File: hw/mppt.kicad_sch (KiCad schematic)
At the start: 0 parts

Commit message: working on documentation, design methmethodology, sizing, layout
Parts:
- added H101: Top Left Mounting Hole, MountingHole:MountingHole_2.2mm_M2, symbol Mechanical:MountingHole
- added H102: Top Right Mounting Hole, MountingHole:MountingHole_2.2mm_M2, symbol Mechanical:MountingHole
- added H103: Bottom Left Mounting Hole, MountingHole:MountingHole_2.2mm_M2, symbol Mechanical:MountingHole
- added H104: Bottom Right Mounting Hole, MountingHole:MountingHole_2.2mm_M2, symbol Mechanical:MountingHole
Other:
- sheet controller ports: added ARR_CURRENT, ARR_VOLTAGE, BATT_CURRENT, BATT_VOLTAGE, PWM; removed none
- sheet converter ports: added SW1, SW2, V_ARR+, V_ARR-, V_BATT+, V_BATT-; removed none
- sheet sensors ports: added +ARR, +BATT, -ARR, -BATT, ARRAY_CURRENT, ARRAY_VOLTAGE, BATTERY_CURRENT, BATTERY_VOLTAGE; removed none

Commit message: parts of gate driver
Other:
- sheet controller ports: added PWM_EN; removed none
- sheet gate_driver ports: added PWM, PWM_EN, SW1_OUT, SW2_OUT; removed none
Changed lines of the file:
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@@
     (comment 3 "Matthew Yu")
   )
+  (wire (pts (xy 81.28 72.39) (xy 83.82 72.39))
+    (stroke (width 0) (type default))
+  )
   (wire (pts (xy 34.29 45.72) (xy 31.75 45.72))
     (stroke (width 0) (type default))
   )
+  (wire (pts (xy 83.82 57.15) (xy 81.28 57.15))
+    (stroke (width 0) (type default))
+  )
+  (wire (pts (xy 83.82 54.61) (xy 80.01 54.61))
+    (stroke (width 0) (type default))
+  )
   (wire (pts (xy 29.21 40.64) (xy 29.21 73.66))
     (stroke (width 0) (type default))
@@
     (stroke (width 0) (type default))
   )
+  (wire (pts (xy 72.39 38.1) (xy 83.82 38.1))
+    (stroke (width 0) (type default))
+  )
   (wire (pts (xy 31.75 78.74) (xy 34.29 78.74))
     (stroke (width 0) (type default))
   )
+  (wire (pts (xy 80.01 54.61) (xy 80.01 69.85))
+    (stroke (width 0) (type default))
+  )
   (wire (pts (xy 72.39 83.82) (xy 83.82 83.82))
     (stroke (width 0) (type default))
@@
     (stroke (width 0) (type default))
   )
+  (wire (pts (xy 81.28 57.15) (xy 81.28 72.39))
+    (stroke (width 0) (type default))
+  )
   (wire (pts (xy 72.39 76.2) (xy 83.82 76.2))
     (stroke (width 0) (type default))
@@
     (stroke (width 0) (type default))
   )
+  (wire (pts (xy 72.39 40.64) (xy 83.82 40.64))
+    (stroke (width 0) (type default))
+  )
   (wire (pts (xy 34.29 71.12) (xy 27.94 71.12))
+    (stroke (width 0) (type default))
+  )
+  (wire (pts (xy 80.01 69.85) (xy 83.82 69.85))
     (stroke (width 0) (type default))
   )
@@
       (effects (font (size 1.27 1.27)) (justify left))
     )
-    (pin "PWM" input (at 34.29 49.53 180)
-      (effects (font (size 1.27 1.27)) (justify left))
+    (pin "PWM" input (at 72.39 38.1 0)
+      (effects (font (size 1.27 1.27)) (justify right))
+    )
+    (pin "PWM_EN" input (at 72.39 40.64 0)
+      (effects (font (size 1.27 1.27)) (justify right))
     )
     (instances
@@
       (effects (font (size 1.27 1.27)) (justify left top))
     )
-    (instances
+    (pin "PWM" input (at 83.82 38.1 180)
+      (effects (font (size 1.27 1.27)) (justify left))
+    )
+    (pin "PWM_EN" input (at 83.82 40.64 180)
+      (effects (font (size 1.27 1.27)) (justify left))
+    )
+    (pin "SW1_OUT" input (at 83.82 54.61 180)
+      (effects (font (size 1.27 1.27)) (justify left))
+    )
+    (pin "SW2_OUT" input (at 83.82 57.15 180)
+      (effects (font (size 1.27 1.27)) (justify left))
+    )
+    (instances

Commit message: layout revision this one is cursed
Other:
- sheet converter ports: added V_SW; removed none
- sheet gate_driver ports: added V_SW; removed none
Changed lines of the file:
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@@
+    (stroke (width 0) (type default))
+  )
+  (wire (pts (xy 125.73 69.85) (xy 121.92 69.85))
+    (stroke (width 0) (type default))
+  )
+  (wire (pts (xy 121.92 57.15) (xy 125.73 57.15))
     (stroke (width 0) (type default))
   )
@@
   )
   (wire (pts (xy 30.48 43.18) (xy 30.48 76.2))
+    (stroke (width 0) (type default))
+  )
+  (wire (pts (xy 125.73 57.15) (xy 125.73 69.85))
     (stroke (width 0) (type default))
   )
@@
       (effects (font (size 1.27 1.27)) (justify left))
     )
+    (pin "V_SW" input (at 121.92 69.85 0)
+      (effects (font (size 1.27 1.27)) (justify right))
+    )
     (instances
       (project "mppt"
@@
       (effects (font (size 1.27 1.27)) (justify left))
     )
-    (instances
+    (pin "V_SW" input (at 121.92 57.15 0)
+      (effects (font (size 1.27 1.27)) (justify right))
+    )
+    (instances

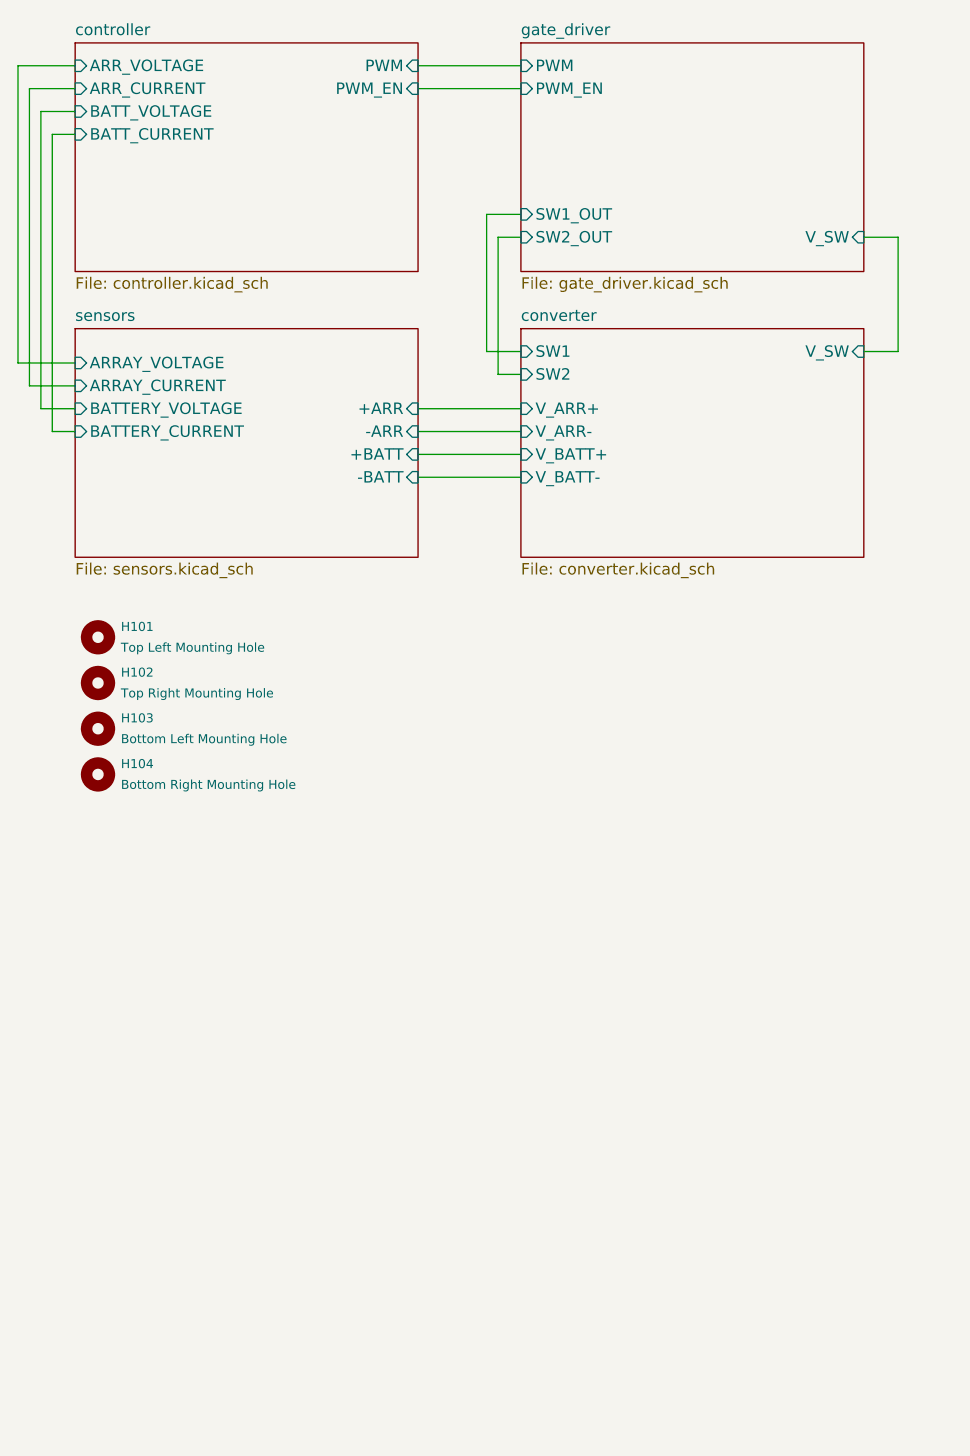
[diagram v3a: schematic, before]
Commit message: segregating code into design procedures
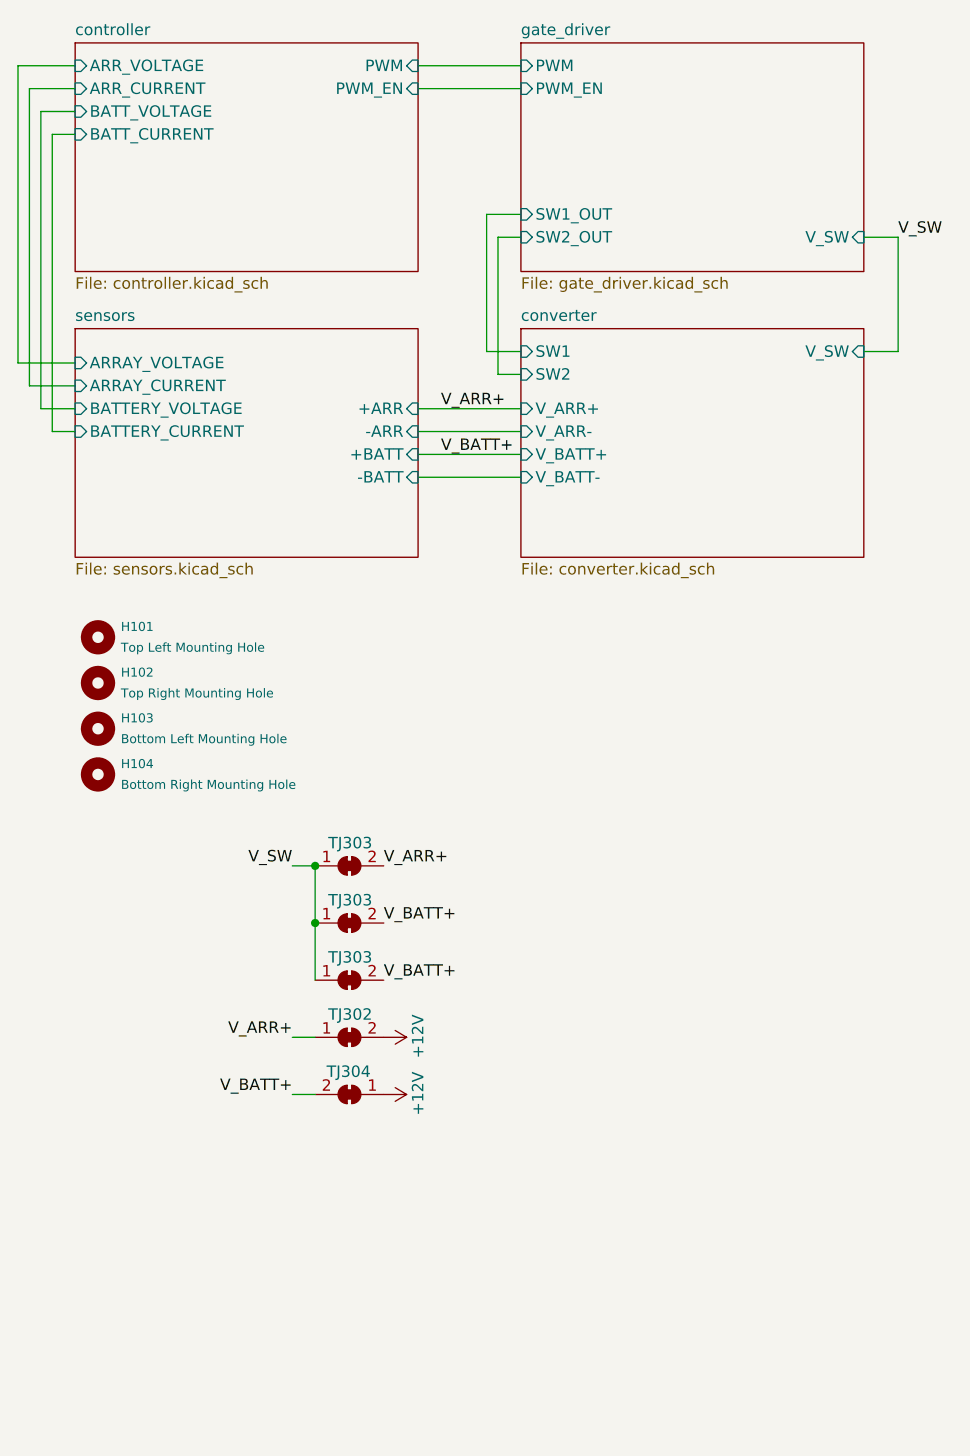
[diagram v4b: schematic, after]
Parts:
- added TJ302, TJ303 (x3), TJ304: Thermal Jumper, Resistor_SMD:R_0805_2012Metric, symbol Jumper:SolderJumper_2_Bridged
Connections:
- new net +12V: TJ302.2 (B), TJ304.1 (A)
- new net V_ARR+: TJ302.1 (A), TJ303.2 (B)
- new net V_BATT+: TJ303.2 (B), TJ303.2 (B), TJ304.2 (B)
- new net V_SW: TJ303.1 (A), TJ303.1 (A), TJ303.1 (A)

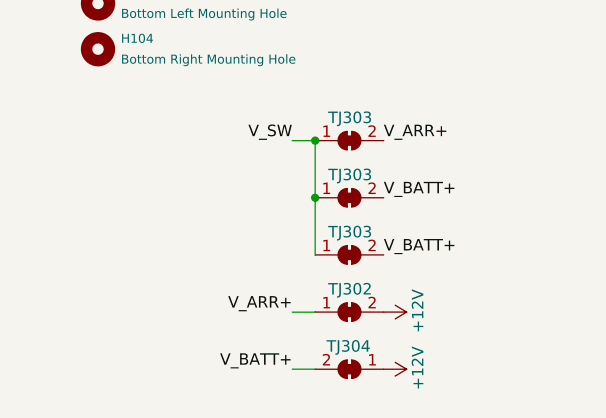
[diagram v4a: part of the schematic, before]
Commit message: added Vsw test point and altered Vsw trace slightly
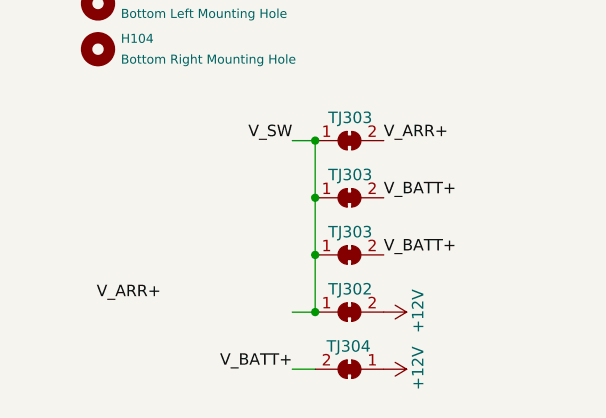
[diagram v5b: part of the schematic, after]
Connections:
- net V_ARR+: no longer TJ302.1 (A)
- net V_SW: now also TJ302.1 (A)
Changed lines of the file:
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@@
     (comment 3 "Matthew Yu")
+  )
+  (junction (at 60.96 139.7) (diameter 0) (color 0 0 0 0)
   )
   (junction (at 60.96 133.35) (diameter 0) (color 0 0 0 0)
   )
+  (junction (at 60.96 146.05) (diameter 0) (color 0 0 0 0)
+  )
   (junction (at 60.96 127) (diameter 0) (color 0 0 0 0)
+  )
+  (wire (pts (xy 60.96 139.7) (xy 60.96 146.05))
+    (stroke (width 0) (type default))
   )
   (wire (pts (xy 60.96 133.35) (xy 60.96 139.7))
@@
     (effects (font (size 1.27 1.27)) (justify left bottom))
   )
-  (label "V_ARR+" (at 58.42 146.05 180) (fields_autoplaced)
+  (label "V_ARR+" (at 43.815 144.78 180) (fields_autoplaced)
     (effects (font (size 1.27 1.27)) (justify right bottom))
   )
